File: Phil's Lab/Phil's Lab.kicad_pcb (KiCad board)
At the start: 2 copper layers, 41 x 31 mm, 32 parts, among them J1 USB_B_Micro, J2 Conn_01x04, J3 Conn_01x04, J4 Conn_01x04, SW1 SW_SPDT, U1 AMS1117-3.3, U2 STM32F103C8T6, Y1 16MHz

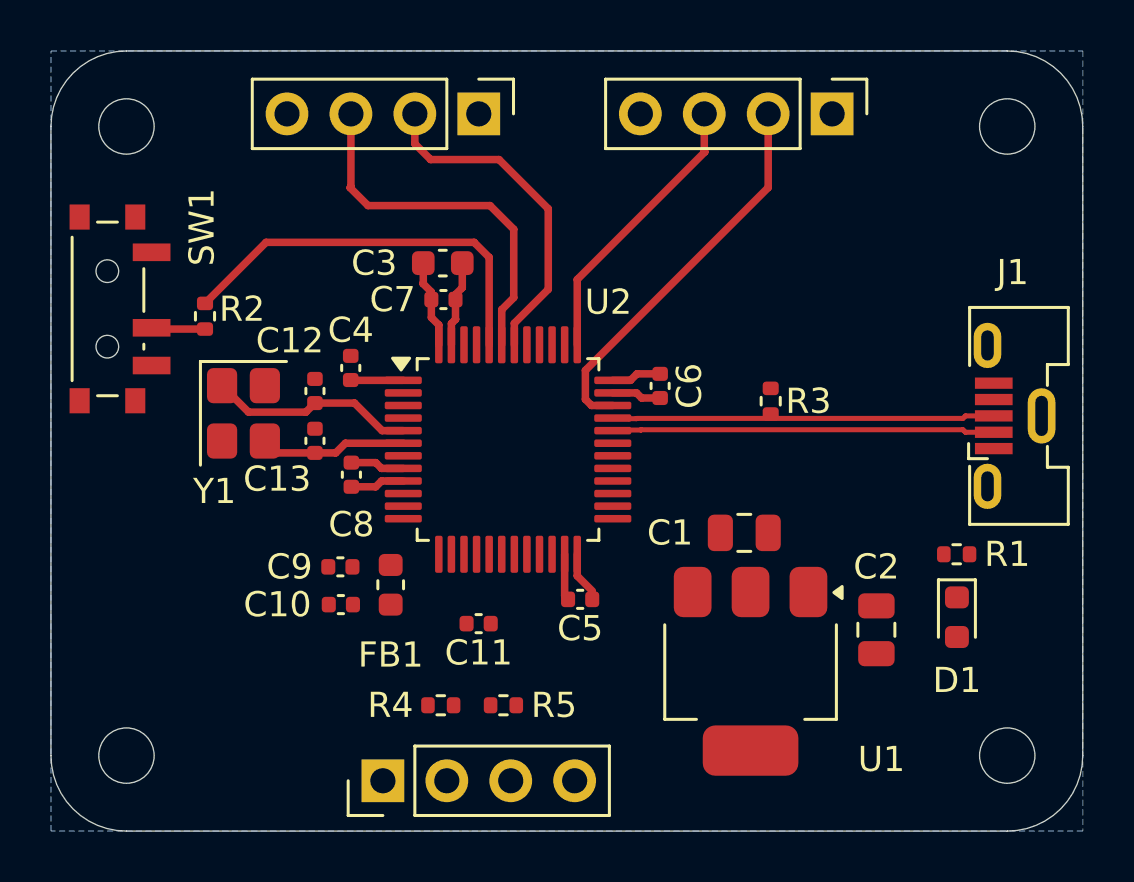
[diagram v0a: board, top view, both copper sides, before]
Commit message: Adjust PCB footprints, add routing and backups
Apply multiple footprint refinements and add routing: updated many component positions, pad rotations and silk/text coordinates (and several UUID updates) in Phil's Lab.kicad_pcb; added extensive F.Cu traces, vias and segments to complete routing for multiple nets. Also add several timestamped backup ZIPs and KiCad lock files (~Phil's Lab.kicad_pcb.lck, ~Phil's Lab.kicad_sch.lck). These changes finalize placement adjustments and implement board routing.
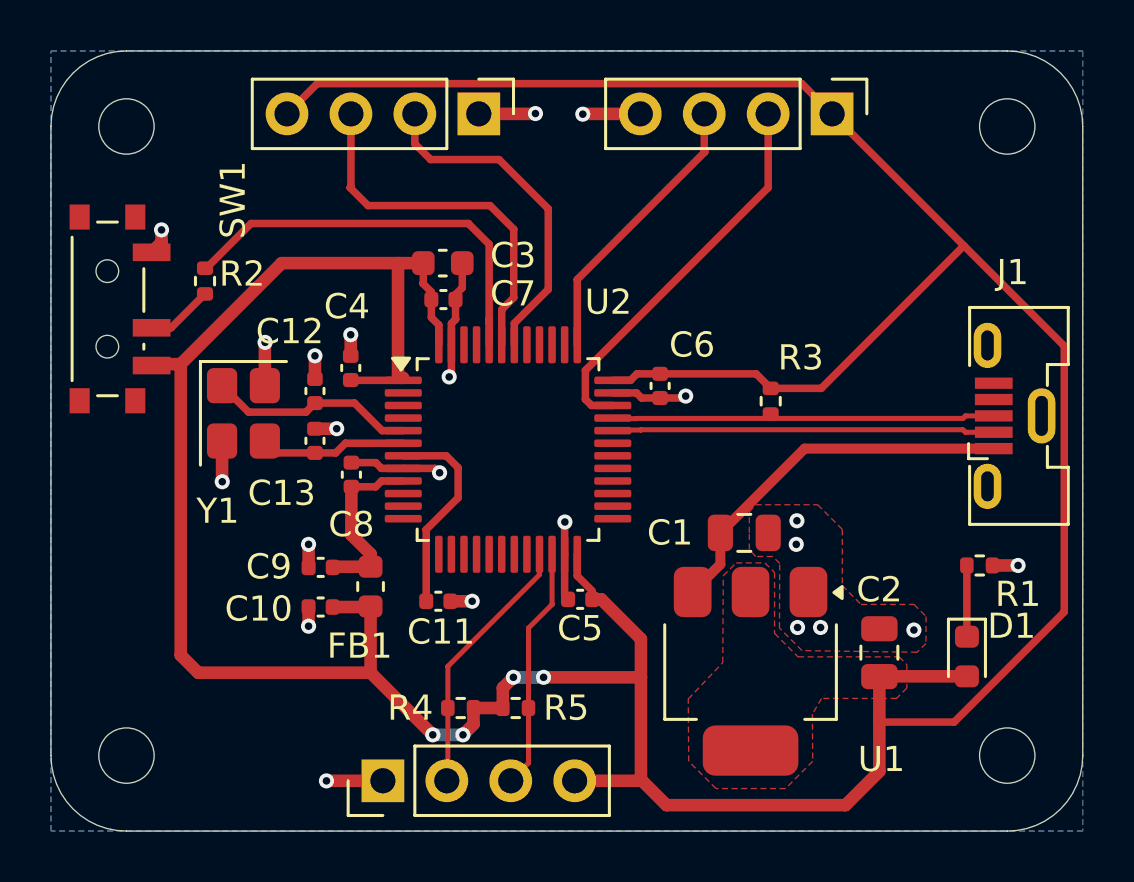
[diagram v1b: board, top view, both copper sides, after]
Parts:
- moved C11 1.83 mm to (51.9, 69.4), turned to 0 degrees
- moved D1 1.61 mm to (72.9, 71.6)
- moved R2 1.40 mm to (42.6, 56.6)
- moved R1 1.02 mm to (73.4, 67.9), turned to 0 degrees
- moved C2 0.92 mm to (69.4, 71.4)
- moved C10 0.81 mm to (47.2, 69.6), turned to 180 degrees
- moved FB1 0.80 mm to (49.2, 68.8)
- moved R4 0.80 mm to (52.8, 73.6)
- moved C9 0.78 mm to (47.2, 68.0), turned to 180 degrees
- moved R5 0.50 mm to (55.0, 73.6)
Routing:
- net +3.3V: track 9.30 -> 162.2 mm, vias 0 -> 4
- net GND: track 9.40 -> 32.0 mm, vias 0 -> 17
- net VBUS: track 0.00 -> 15.1 mm
- net /I2C2_SCL: track 0.00 -> 10.5 mm
- net /I2C2_SDA: track 0.00 -> 9.68 mm
- net /NRST: track 0.00 -> 8.21 mm
- net +3.3VA: track 2.16 -> 7.16 mm
- net /PWR_LED_K: track 0.00 -> 2.83 mm
- net /SW_BOOT0: track 2.14 -> 2.75 mm
- net /BOOT0: track 16.0 -> 16.5 mm
- net (no net): vias 0 -> 5
- added copper zone on F.Cu, net +3.3V
- added copper zone on F.Cu, net GND

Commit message: Small Update
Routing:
- net GND: track 32.0 -> 26.7 mm, vias 17 -> 20
- net (no net): vias 5 -> 0
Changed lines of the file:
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@@
 		(layer "Edge.Cuts")
-	)
-	(via
-		(at 66.1162 67.1068)
-		(size 0.6)
-		(drill 0.3)
-		(layers "F.Cu" "B.Cu")
-		(net 0)
-	)
-	(via
-		(at 70.7898 70.5104)
-		(size 0.6)
-		(drill 0.3)
-		(layers "F.Cu" "B.Cu")
-		(net 0)
-	)
-	(via
-		(at 66.167 70.4088)
-		(size 0.6)
-		(drill 0.3)
-		(layers "F.Cu" "B.Cu")
-		(net 0)
-	)
-	(via
-		(at 67.0814 70.4088)
-		(size 0.6)
-		(drill 0.3)
-		(layers "F.Cu" "B.Cu")
-		(net 0)
-	)
-	(via
-		(at 66.1416 66.167)
-		(size 0.6)
-		(drill 0.3)
-		(layers "F.Cu" "B.Cu")
-		(net 0)
 	)
 	(segment
@@
 	)
 	(segment
-		(start 49.69 76.5)
-		(end 47.452 76.5)
-		(width 0.5)
-		(layer "F.Cu")
-		(net 2)
-	)
-	(segment
 		(start 50.5 64.0875)
 		(end 51.7685 64.0875)
@@
 	)
 	(segment
-		(start 57.6452 50)
-		(end 57.6326 50.0126)
-		(width 0.5)
-		(layer "F.Cu")
-		(net 2)
-	)
-	(segment
-		(start 59.92 50)
-		(end 57.6452 50)
-		(width 0.5)
-		(layer "F.Cu")
-		(net 2)
-	)
-	(segment
 		(start 45 60.8)
 		(end 45 59.0892)
@@
 	)
 	(segment
+		(start 72.39 60.7014)
+		(end 73.9648 60.7014)
+		(width 0.4)
+		(layer "F.Cu")
+		(net 2)
+	)
+	(segment
 		(start 61.6458 61.2902)
 		(end 61.722 61.214)
@@
 	)
 	(segment
-		(start 53.5 50)
-		(end 55.7402 50)
-		(width 0.5)
-		(layer "F.Cu")
-		(net 2)
-	)
-	(segment
 		(start 47.851 62.512)
 		(end 47.8536 62.5094)
@@
 	)
 	(segment
-		(start 55.7402 50)
-		(end 55.753 49.9872)
-		(width 0.5)
-		(layer "F.Cu")
-		(net 2)
-	)
-	(segment
 		(start 46.7386 67.1094)
 		(end 46.736 67.1068)
@@
 	)
 	(segment
-		(start 47.452 76.5)
-		(end 47.4472 76.5048)
-		(width 0.5)
-		(layer "F.Cu")
-		(net 2)
-	)
-	(segment
 		(start 60.706 61.2902)
 		(end 61.6458 61.2902)
@@
 	)
 	(via
+		(at 66.1162 67.1068)
+		(size 0.6)
+		(drill 0.3)
+		(layers "F.Cu" "B.Cu")
+		(free yes)
+		(net 2)
+	)
+	(via
 		(at 48.4124 58.7756)
 		(size 0.6)
@@
 	)
 	(via
-		(at 55.753 49.9872)
-		(size 0.6)
-		(drill 0.3)
-		(layers "F.Cu" "B.Cu")
+		(at 70.7898 70.5104)
+		(size 0.6)
+		(drill 0.3)
+		(layers "F.Cu" "B.Cu")
+		(free yes)
+		(net 2)
+	)
+	(via
+		(at 66.167 70.4088)
+		(size 0.6)
+		(drill 0.3)
+		(layers "F.Cu" "B.Cu")
+		(free yes)
 		(net 2)
 	)
@@
 	)
 	(via
+		(at 67.0814 70.4088)
+		(size 0.6)
+		(drill 0.3)
+		(layers "F.Cu" "B.Cu")
+		(free yes)
+		(net 2)
+	)
+	(via
 		(at 47.8536 62.5094)
 		(size 0.6)
@@
 	)
 	(via
-		(at 57.6326 50.0126)
-		(size 0.6)
-		(drill 0.3)
-		(layers "F.Cu" "B.Cu")
-		(net 2)
-	)
-	(via
 		(at 52.324 60.452)
 		(size 0.6)
@@
 	)
 	(via
-		(at 47.4472 76.5048)
+		(at 72.39 60.7014)
 		(size 0.6)
 		(drill 0.3)
@@
 		(net 2)
 	)
+	(via
+		(at 66.1416 66.167)
+		(size 0.6)
+		(drill 0.3)
+		(layers "F.Cu" "B.Cu")
+		(free yes)
+		(net 2)
+	)
